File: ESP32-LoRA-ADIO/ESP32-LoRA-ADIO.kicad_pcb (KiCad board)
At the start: 2 copper layers, 93 x 61 mm, 27 parts, among them J1 USB_B_Micro, J2 External Power, J3 AIO/I2C, J4 DIO, J5 RXTX+Power, J6 SMA, Q1 IRLML5203, Q2 2N7002, Q3 2N7002, U1 AP1117-33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

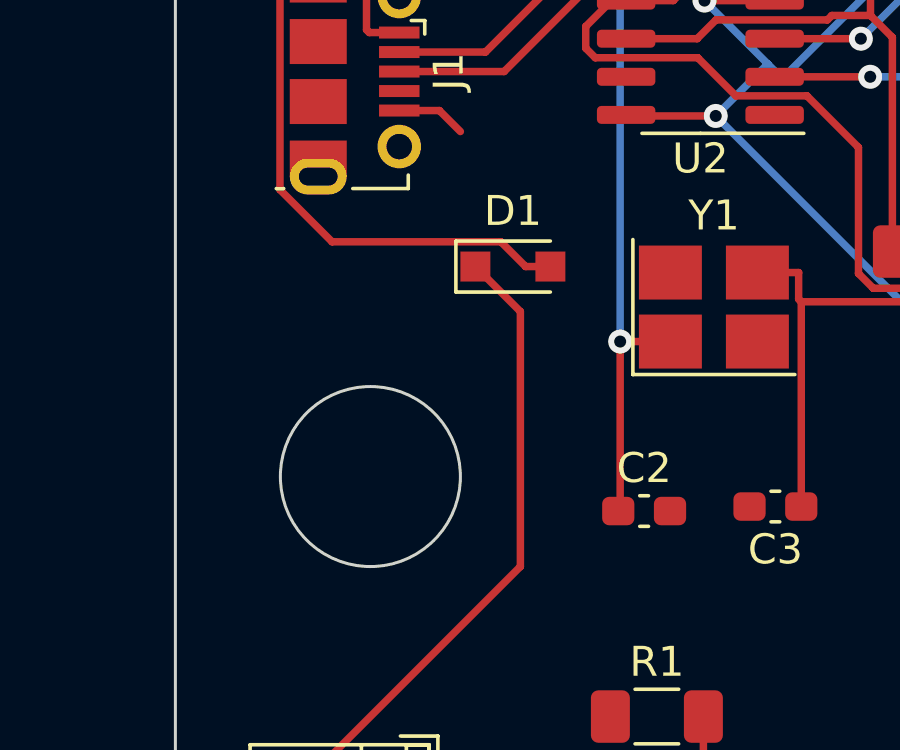
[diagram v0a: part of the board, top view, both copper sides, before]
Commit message: Rotated the schottky diode for the next Revision
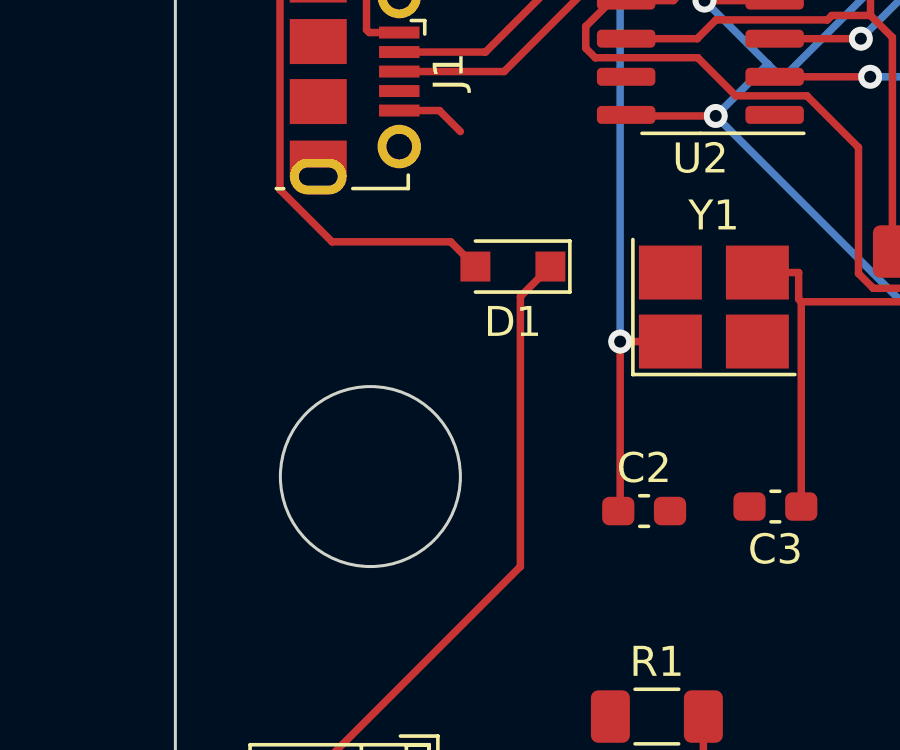
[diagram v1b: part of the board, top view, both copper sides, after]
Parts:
- turned D1 to 180 degrees
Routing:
- net Net-(D1-Pad2): track 24.7 -> 22.2 mm
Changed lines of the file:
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@@
   )
   (footprint "Diode_SMD:D_SOD-323_HandSoldering" (layer "F.Cu")
-    (at 125.25 49.5)
+    (at 125.25 49.5 180)
     (descr "SOD-323")
     (tags "SOD-323")
@@
     (fp_line (start 0.9 -0.7) (end 0.9 0.7) (layer "F.Fab") (width 0.1))
     (fp_line (start 0.2 0.35) (end -0.3 0) (layer "F.Fab") (width 0.1))
-    (pad "1" smd rect (at -1.25 0) (size 1 1) (layers "F.Cu" "F.Paste" "F.Mask")
+    (pad "1" smd rect (at -1.25 0 180) (size 1 1) (layers "F.Cu" "F.Paste" "F.Mask")
       (net 1 "+5V") (pinfunction "K") (pintype "passive"))
-    (pad "2" smd rect (at 1.25 0) (size 1 1) (layers "F.Cu" "F.Paste" "F.Mask")
+    (pad "2" smd rect (at 1.25 0 180) (size 1 1) (layers "F.Cu" "F.Paste" "F.Mask")
       (net 6 "Net-(D1-Pad2)") (pinfunction "A") (pintype "passive"))
     (model "${KICAD6_3DMODEL_DIR}/Diode_SMD.3dshapes/D_SOD-323.wrl"
@@
   (segment (start 145.8029 66.8) (end 147.2 66.8) (width 0.25) (layer "F.Cu") (net 1))
   (segment (start 145.8029 61.3369) (end 149.1398 58) (width 0.25) (layer "F.Cu") (net 1))
-  (segment (start 125.5 59.5) (end 125.5 51) (width 0.25) (layer "F.Cu") (net 1))
   (segment (start 128.5625 70.9625) (end 132.725 66.8) (width 0.25) (layer "F.Cu") (net 1))
-  (segment (start 119.1058 69.3071) (end 118.6267 68.828) (width 0.25) (layer "F.Cu") (net 1))
+  (segment (start 125.5 59.5) (end 125.5 50.5) (width 0.25) (layer "F.Cu") (net 1))
   (segment (start 145.8029 66.8) (end 145.8029 61.3369) (width 0.25) (layer "F.Cu") (net 1))
   (segment (start 149.1398 58) (end 149.6375 58) (width 0.25) (layer "F.Cu") (net 1))
+  (segment (start 125.5 50.5) (end 126.5 49.5) (width 0.25) (layer "F.Cu") (net 1))
+  (segment (start 132.725 66.8) (end 145.8029 66.8) (width 0.25) (layer "F.Cu") (net 1))
+  (segment (start 118.6267 66.3733) (end 125.5 59.5) (width 0.25) (layer "F.Cu") (net 1))
+  (segment (start 128.5625 71.45) (end 128.5625 70.9625) (width 0.25) (layer "F.Cu") (net 1))
   (segment (start 128.5625 70.9625) (end 126.9071 69.3071) (width 0.25) (layer "F.Cu") (net 1))
+  (segment (start 119.1058 69.3071) (end 118.6267 68.828) (width 0.25) (layer "F.Cu") (net 1))
   (segment (start 118.6267 68.828) (end 118.6267 66.3733) (width 0.25) (layer "F.Cu") (net 1))
-  (segment (start 132.725 66.8) (end 145.8029 66.8) (width 0.25) (layer "F.Cu") (net 1))
-  (segment (start 125.5 51) (end 124 49.5) (width 0.25) (layer "F.Cu") (net 1))
-  (segment (start 128.5625 71.45) (end 128.5625 70.9625) (width 0.25) (layer "F.Cu") (net 1))
-  (segment (start 118.6267 66.3733) (end 125.5 59.5) (width 0.25) (layer "F.Cu") (net 1))
   (segment (start 126.9071 69.3071) (end 119.1058 69.3071) (width 0.25) (layer "F.Cu") (net 1))
   (segment (start 149.725 39.225) (end 151 40.5) (width 0.25) (layer "F.Cu") (net 2))
@@
   (segment (start 134.2331 43.2314) (end 143.9017 33.5628) (width 0.25) (layer "B.Cu") (net 5))
   (segment (start 133.7466 42.7449) (end 131.6366 40.635) (width 0.25) (layer "B.Cu") (net 5))
-  (segment (start 124.8494 48.6747) (end 125.6747 49.5) (width 0.25) (layer "F.Cu") (net 6))
   (segment (start 117.9515 38.5696) (end 117.4868 39.0343) (width 0.25) (layer "F.Cu") (net 6))
-  (segment (start 126.5 49.5) (end 125.6747 49.5) (width 0.25) (layer "F.Cu") (net 6))
+  (segment (start 120.4622 41.7) (end 120.3708 41.6086) (width 0.25) (layer "F.Cu") (net 6))
+  (segment (start 119.2226 48.6747) (end 123.1747 48.6747) (width 0.25) (layer "F.Cu") (net 6))
+  (segment (start 119.4993 38.5696) (end 117.9515 38.5696) (width 0.25) (layer "F.Cu") (net 6))
+  (segment (start 123.1747 48.6747) (end 124 49.5) (width 0.25) (layer "F.Cu") (net 6))
+  (segment (start 117.4868 46.9389) (end 119.2226 48.6747) (width 0.25) (layer "F.Cu") (net 6))
+  (segment (start 120.3708 39.4411) (end 119.4993 38.5696) (width 0.25) (layer "F.Cu") (net 6))
+  (segment (start 120.3708 41.6086) (end 120.3708 39.4411) (width 0.25) (layer "F.Cu") (net 6))
   (segment (start 117.4868 39.0343) (end 117.4868 46.9389) (width 0.25) (layer "F.Cu") (net 6))
   (segment (start 121.4625 41.7) (end 120.4622 41.7) (width 0.25) (layer "F.Cu") (net 6))
-  (segment (start 119.2226 48.6747) (end 124.8494 48.6747) (width 0.25) (layer "F.Cu") (net 6))
-  (segment (start 119.4993 38.5696) (end 117.9515 38.5696) (width 0.25) (layer "F.Cu") (net 6))
-  (segment (start 120.3708 39.4411) (end 119.4993 38.5696) (width 0.25) (layer "F.Cu") (net 6))
-  (segment (start 117.4868 46.9389) (end 119.2226 48.6747) (width 0.25) (layer "F.Cu") (net 6))
-  (segment (start 120.4622 41.7) (end 120.3708 41.6086) (width 0.25) (layer "F.Cu") (net 6))
-  (segment (start 120.3708 41.6086) (end 120.3708 39.4411) (width 0.25) (layer "F.Cu") (net 6))
   (segment (start 133.975 38.095) (end 133.3398 38.7302) (width 0.25) (layer "F.Cu") (net 7))
   (segment (start 124.3371 42.35) (end 121.4625 42.35) (width 0.25) (layer "F.Cu") (net 7))

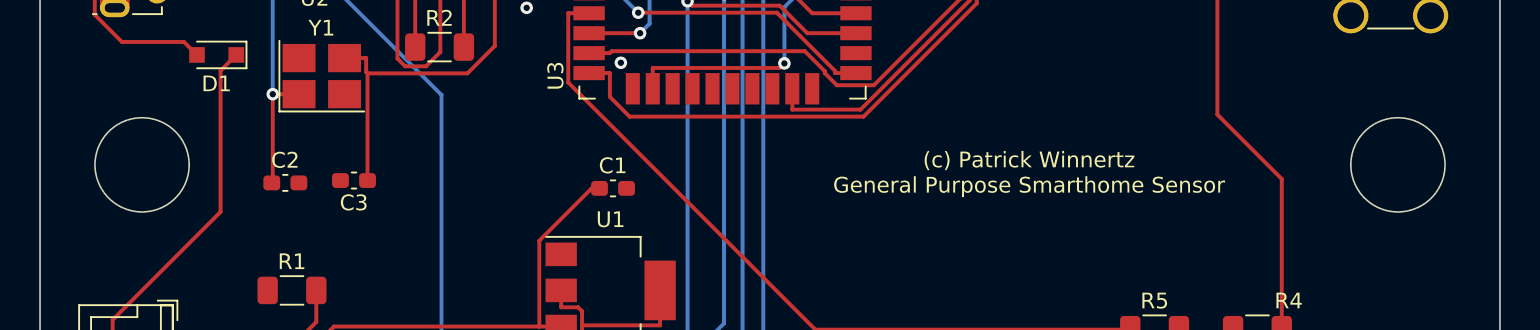
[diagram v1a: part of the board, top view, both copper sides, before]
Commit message: Change PCB layout a bit to fit better into the case
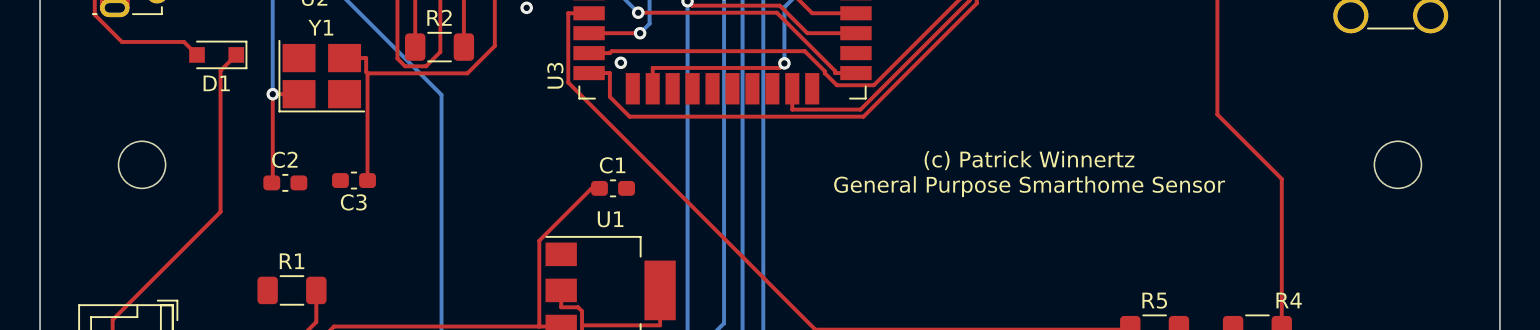
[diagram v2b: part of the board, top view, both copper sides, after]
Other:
- outline, holes or cut-outs redrawn
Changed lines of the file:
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@@
       (xy 196 26)
     ) (layer "Edge.Cuts") (width 0.1) (fill none))
-  (gr_circle (center 200.5 56.5) (end 203.5 56.5) (layer "Edge.Cuts") (width 0.1) (fill none))
-  (gr_circle (center 120.5 56.5) (end 123.5 56.5) (layer "Edge.Cuts") (width 0.1) (fill none))
+  (gr_circle (center 200.5 56.5) (end 202 56.5) (layer "Edge.Cuts") (width 0.1) (fill none))
+  (gr_circle (center 120.5 56.5) (end 122 56.5) (layer "Edge.Cuts") (width 0.1) (fill none))
   (gr_text "(c) Patrick Winnertz\nGeneral Purpose Smarthome Sensor" (at 177 57) (layer "F.SilkS")
     (effects (font (size 1 1) (thickness 0.25)))
@@
   (segment (start 166.271 52.9803) (end 161.92 52.9803) (width 0.25) (layer "F.Cu") (net 61))
   (segment (start 173.2244 38.9503) (end 173.2244 46.0269) (width 0.25) (layer "F.Cu") (net 61))
+  (zone (net 0) (net_name "") (layers F&B.Cu) (hatch edge 0.508)
+    (connect_pads (clearance 0))
+    (min_thickness 0.254)
+    (keepout (tracks not_allowed) (vias not_allowed) (pads not_allowed ) (copperpour not_allowed) (footprints allowed))
+    (fill (thermal_gap 0.508) (thermal_bridge_width 0.508))
+    (polygon
+      (pts
+        (xy 203.5 59.5)
+        (xy 197.5 59.5)
+        (xy 197.5 53.5)
+        (xy 203.5 53.5)
+      )
+    )
+  )
+  (zone (net 0) (net_name "") (layers F&B.Cu) (hatch edge 0.508)
+    (connect_pads (clearance 0))
+    (min_thickness 0.254)
+    (keepout (tracks not_allowed) (vias not_allowed) (pads not_allowed ) (copperpour not_allowed) (footprints allowed))
+    (fill (thermal_gap 0.508) (thermal_bridge_width 0.508))
+    (polygon
+      (pts
+        (xy 123.5 59.5)
+        (xy 117.5 59.5)
+        (xy 117.5 53.5)
+        (xy 123.5 53.5)
+      )
+    )
+  )
   (zone (net 2) (net_name "Earth") (layers F&B.Cu) (hatch edge 0.508)
     (connect_pads (clearance 0.508))
